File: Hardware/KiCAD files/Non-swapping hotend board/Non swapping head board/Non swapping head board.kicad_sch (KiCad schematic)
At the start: 3 parts, among them J18 JST_1mm_3_Vertical, J20 PINHD_1x10_Female, J22 Conn_01x02

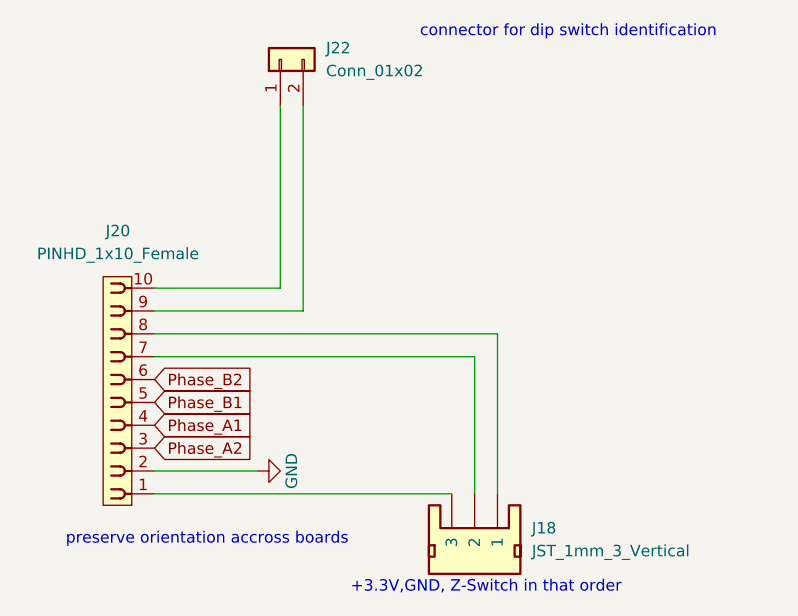
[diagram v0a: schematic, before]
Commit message: Hotfix to create non-swapping board
hotfix on non-swapping done, swapping board is mapped for completion after CAD modeling phase begins
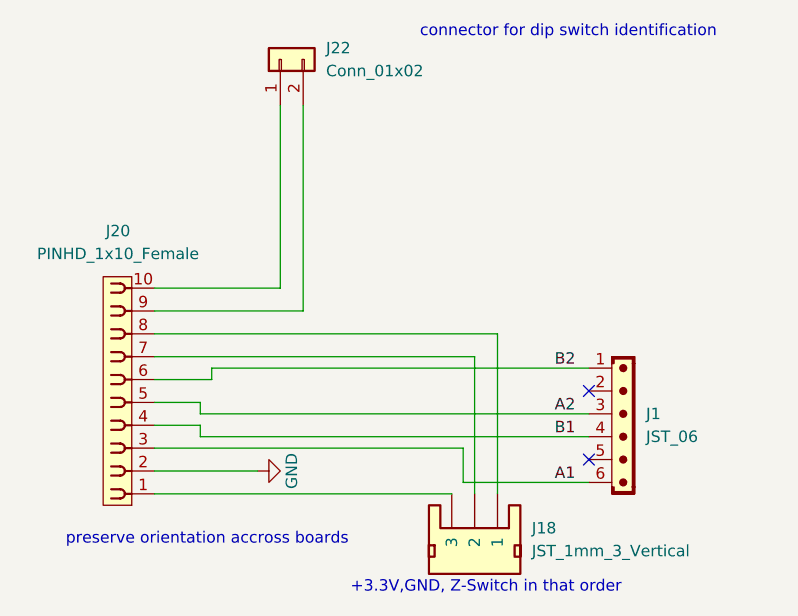
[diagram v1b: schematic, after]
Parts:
- added J1: JST_06, Connector_JST:JST_EH_B6B-EH-A_1x06_P2.50mm_Vertical, symbol PCM_SL_Connectors:JST_06
- J20: footprint Connector_PinSocket_2.54mm:PinSocket_1x10_P2.54mm_Vertical -> Connector_PinSocket_2.54mm:PinSocket_1x10_P2.54mm_Horizontal
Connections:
- net Phase_A1 renamed B1
- net B1: now also J1.4
- net Phase_A2 renamed A1
- net A1: now also J1.6
- net Phase_B1 renamed A2
- net A2: now also J1.3
- net Phase_B2 renamed B2
- net B2: now also J1.1
- no-connect marks 0 -> 2
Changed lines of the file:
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@@
+		)
+	)
+	(no_connect
+		(at 81.28 58.42)
+	)
+	(no_connect
+		(at 81.28 66.04)
+	)
+	(wire
+		(pts
+			(xy 81.28 60.96) (xy 38.1 60.96)
+		)
+		(stroke
+			(width 0)
+			(type default)
 		)
 	)
@@
 	(wire
 		(pts
+			(xy 39.37 55.88) (xy 39.37 57.15)
+		)
+		(stroke
+			(width 0)
+			(type default)
+		)
+	)
+	(wire
+		(pts
 			(xy 33.02 49.53) (xy 49.53 49.53)
 		)
@@
 	(wire
 		(pts
+			(xy 39.37 55.88) (xy 81.28 55.88)
+		)
+		(stroke
+			(width 0)
+			(type default)
+		)
+	)
+	(wire
+		(pts
+			(xy 81.28 63.5) (xy 38.1 63.5)
+		)
+		(stroke
+			(width 0)
+			(type default)
+		)
+	)
+	(wire
+		(pts
 			(xy 33.02 52.07) (xy 71.12 52.07)
 		)
@@
 	(wire
 		(pts
+			(xy 33.02 59.69) (xy 38.1 59.69)
+		)
+		(stroke
+			(width 0)
+			(type default)
+		)
+	)
+	(wire
+		(pts
 			(xy 71.12 52.07) (xy 71.12 69.85)
 		)
@@
 	(wire
 		(pts
+			(xy 67.31 64.77) (xy 33.02 64.77)
+		)
+		(stroke
+			(width 0)
+			(type default)
+		)
+	)
+	(wire
+		(pts
+			(xy 39.37 57.15) (xy 33.02 57.15)
+		)
+		(stroke
+			(width 0)
+			(type default)
+		)
+	)
+	(wire
+		(pts
 			(xy 68.58 69.85) (xy 68.58 54.61)
 		)
@@
 	(wire
 		(pts
+			(xy 81.28 68.58) (xy 67.31 68.58)
+		)
+		(stroke
+			(width 0)
+			(type default)
+		)
+	)
+	(wire
+		(pts
+			(xy 67.31 68.58) (xy 67.31 64.77)
+		)
+		(stroke
+			(width 0)
+			(type default)
+		)
+	)
+	(wire
+		(pts
 			(xy 33.02 67.31) (xy 44.45 67.31)
 		)
@@
 		)
 	)
-	(global_label "Phase_A2"
-		(shape input)
-		(at 33.02 64.77 0)
-		(fields_autoplaced yes)
+	(wire
+		(pts
+			(xy 33.02 62.23) (xy 38.1 62.23)
+		)
+		(stroke
+			(width 0)
+			(type default)
+		)
+	)
+	(wire
+		(pts
+			(xy 38.1 60.96) (xy 38.1 59.69)
+		)
+		(stroke
+			(width 0)
+			(type default)
+		)
+	)
+	(wire
+		(pts
+			(xy 38.1 63.5) (xy 38.1 62.23)
+		)
+		(stroke
+			(width 0)
+			(type default)
+		)
+	)
+	(label "B2"
+		(at 77.47 55.88 0)
 		(effects
 			(font
 				(size 1.27 1.27)
 			)
-			(justify left)
-		)
-		(property "Intersheetrefs" "${INTERSHEET_REFS}"
-			(at 44.9556 64.77 0)
-			(hide yes)
-			(show_name no)
-			(do_not_autoplace no)
-			(effects
-				(font
-					(size 1.27 1.27)
-				)
-				(justify left)
-			)
-		)
-	)
-	(global_label "Phase_B2"
-		(shape input)
-		(at 33.02 57.15 0)
-		(fields_autoplaced yes)
+			(justify left bottom)
+		)
+	)
+	(label "B1"
+		(at 77.47 63.5 0)
 		(effects
 			(font
 				(size 1.27 1.27)
 			)
-			(justify left)
-		)
-		(property "Intersheetrefs" "${INTERSHEET_REFS}"
-			(at 45.137 57.15 0)
-			(hide yes)
-			(show_name no)
-			(do_not_autoplace no)
-			(effects
-				(font
-					(size 1.27 1.27)
-				)
-				(justify left)
-			)
-		)
-	)
-	(global_label "Phase_B1"
-		(shape input)
-		(at 33.02 59.69 0)
-		(fields_autoplaced yes)
+			(justify left bottom)
+		)
+	)
+	(label "A2"
+		(at 77.47 60.96 0)
 		(effects
 			(font
 				(size 1.27 1.27)
 			)
-			(justify left)
-		)
-		(property "Intersheetrefs" "${INTERSHEET_REFS}"
-			(at 45.137 59.69 0)
-			(hide yes)
-			(show_name no)
-			(do_not_autoplace no)
-			(effects
-				(font
-					(size 1.27 1.27)
-				)
-				(justify left)
-			)
-		)
-	)
-	(global_label "Phase_A1"
-		(shape input)
-		(at 33.02 62.23 0)
-		(fields_autoplaced yes)
+			(justify left bottom)
+		)
+	)
+	(label "A1"
+		(at 77.47 68.58 0)
 		(effects
 			(font
 				(size 1.27 1.27)
 			)
-			(justify left)
-		)
-		(property "Intersheetrefs" "${INTERSHEET_REFS}"
-			(at 44.9556 62.23 0)
-			(hide yes)
-			(show_name no)
-			(do_not_autoplace no)
-			(effects
-				(font
-					(size 1.27 1.27)
-				)
-				(justify left)
-			)
+			(justify left bottom)
 		)
 	)
@@
 			)
 		)
-		(property "Footprint" "Connector_PinSocket_2.54mm:PinSocket_1x10_P2.54mm_Vertical"
+		(property "Footprint" "Connector_PinSocket_2.54mm:PinSocket_1x10_P2.54mm_Horizontal"
 			(at 26.67 78.74 0)
 			(hide yes)
@@
 					(unit 1)
 				)
+			)
+		)
+	)
+	(symbol
+		(lib_id "PCM_SL_Connectors:JST_06")
+		(at 85.09 62.23 0)
+		(unit 1)
+		(body_style 1)
+		(exclude_from_sim no)
+		(in_bom yes)
+		(on_board yes)
+		(in_pos_files yes)
+		(dnp no)
+		(fields_autoplaced yes)
+		(property "Reference" "J1"
+			(at 87.63 60.9599 0)
+			(show_name no)
+			(do_not_autoplace no)
+			(effects
+				(font
+					(size 1.27 1.27)
+				)
+				(justify left)
+			)
+		)
+		(property "Value" "JST_06"
+			(at 87.63 63.4999 0)
+			(show_name no)
+			(do_not_autoplace no)
+			(effects
+				(font
+					(size 1.27 1.27)
+				)
+				(justify left)
+			)
+		)
+		(property "Footprint" "Connector_JST:JST_EH_B6B-EH-A_1x06_P2.50mm_Vertical"
+			(at 85.09 50.8 0)
+			(hide yes)
+			(show_name no)
+			(do_not_autoplace no)
+			(effects
+				(font
+					(size 1.27 1.27)
+				)
+			)
+		)
+		(property "Datasheet" ""
+			(at 85.09 50.8 0)
+			(hide yes)
+			(show_name no)
+			(do_not_autoplace no)
+			(effects
+				(font
+					(size 1.27 1.27)
+				)
+			)
+		)
+		(property "Description" "JST Connector  6 pins"
+			(at 85.09 62.23 0)
+			(hide yes)
+			(show_name no)
+			(do_not_autoplace no)
+			(effects
+				(font
+					(size 1.27 1.27)
+				)
+			)
+		)
+		(pin "4"
+		)
+		(pin "1"
+		)
+		(pin "2"
+		)
+		(pin "6"
+		)
+		(pin "3"
+		)
+		(pin "5"
+		)
+		(instances
+			(project "Non swapping head board"
+				(path "/dff84501-92d8-46b4-b4b1-b21350f7bd61"
+					(reference "J1")
+					(unit 1)
+				)

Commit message: V1 boards after final board invoice
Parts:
- J18: footprint PCM_SparkFun-Connector:JST_1x03_P1.0mm_Vertical_SMD -> PCM_SparkFun-Connector:1x03_P2.54mm
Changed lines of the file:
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@@
 			)
 		)
-		(property "Footprint" "PCM_SparkFun-Connector:JST_1x03_P1.0mm_Vertical_SMD"
+		(property "Footprint" "PCM_SparkFun-Connector:1x03_P2.54mm"
 			(at 59.69 74.93 0)
 			(hide yes)
